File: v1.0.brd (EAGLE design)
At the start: 160 x 100 mm, 53 parts, among them J1 DC-044-A, Q3 6pF@32.7680kHz, U1 MCP23017-E/SO, U10 74HC139N, U2 MCP79412-I/SN, U3 LOPY, U4 GROVE_DC&DC, U5 LM1085IT-5.0, X1 JST-XH-05-PIN-ROUND-PAD, X2 JST-XH-05-PIN-ROUND-PAD, X3 JST-XH-05-PIN-ROUND-PAD, X5 JST-XH-05-PIN-ROUND-PAD

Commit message: very minor tweaks
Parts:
- removed R1: 3K, Seeed-Resistor:R0603
- removed R3: 1K, Seeed-Resistor:R0603
- added TP1: TPB2,54, testpad:B2,54
- moved C10 27.1 mm to (-215.9, -312.4), turned to 180 degrees
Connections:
- removed net N$5: R1.2, R3.1, U5.1
- net +5V: now also C10.+, TP1.TP; no longer C10.-, R3.2
- net GND: now also C10.-, U5.1; no longer C10.+, R1.1
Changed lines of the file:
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@@
 <attribute name="MPN" value="CC0603KRX5R6BB106" x="-229.87" y="-309.88" size="1.778" layer="27" display="off"/>
 </element>
-<element name="R1" library="Seeed-Resistor" library_urn="urn:adsk.eagle:library:474" package="R0603" value="3K" x="-234.95" y="-311.15">
-<attribute name="MPN" value="RC0603FR-073KL" x="-234.95" y="-311.15" size="1.778" layer="27" display="off"/>
+<element name="C10" library="Seeed-Capacitor" library_urn="urn:adsk.eagle:library:464" package="AVX-A" value="10uf" x="-215.9" y="-312.42" rot="R180">
+<attribute name="MPN" value="TAJA106K010RNJ" x="-215.9" y="-312.42" size="1.778" layer="27" rot="R180" display="off"/>
 </element>
-<element name="R3" library="Seeed-Resistor" library_urn="urn:adsk.eagle:library:474" package="R0603" value="1K" x="-240.03" y="-311.15">
-<attribute name="MPN" value="RC0603FR-071KL" x="-240.03" y="-311.15" size="1.778" layer="27" display="off"/>
-</element>
-<element name="C10" library="Seeed-Capacitor" library_urn="urn:adsk.eagle:library:464" package="AVX-A" value="10uf" x="-242.57" y="-317.5">
-<attribute name="MPN" value="TAJA106K010RNJ" x="-242.57" y="-317.5" size="1.778" layer="27" display="off"/>
+<element name="TP1" library="testpad" library_urn="urn:adsk.eagle:library:385" package="B2,54" value="TPB2,54" x="-227.33" y="-318.77">
+<attribute name="TP_SIGNAL_NAME" value="" x="-227.33" y="-318.77" size="1.778" layer="27" display="off"/>
 </element>
 </elements>
@@
 <contactref element="X2" pad="3"/>
 <contactref element="X3" pad="3"/>
-<contactref element="R1" pad="1"/>
 <contactref element="C4" pad="1"/>
-<contactref element="C10" pad="+"/>
+<contactref element="U5" pad="1"/>
+<contactref element="C10" pad="-"/>
 <wire x1="-164.719" y1="-102.87" x2="-160.02" y2="-90.678" width="0" layer="19" extent="1-1"/>
 <wire x1="-148.59" y1="-68.58" x2="-160.02" y2="-90.678" width="0" layer="19" extent="1-1"/>
@@
 <wire x1="-213.36" y1="-241.3" x2="-213.36" y2="-226.06" width="0" layer="19" extent="1-1"/>
 <wire x1="-213.36" y1="-256.54" x2="-213.36" y2="-241.3" width="0" layer="19" extent="1-1"/>
+<wire x1="-217.17" y1="-304.546" x2="-213.36" y2="-256.54" width="0" layer="19" extent="1-1"/>
+<wire x1="-217.17" y1="-312.42" x2="-217.17" y2="-304.546" width="0" layer="19" extent="1-1"/>
+<wire x1="-229.87" y1="-309.118" x2="-217.17" y2="-304.546" width="0" layer="19" extent="1-1"/>
 <wire x1="-114.3" y1="4.572" x2="-129.54" y2="-43.688" width="0" layer="19" extent="1-1"/>
-<wire x1="-229.87" y1="-309.118" x2="-213.36" y2="-256.54" width="0" layer="19" extent="1-1"/>
-<wire x1="-234.95" y1="-310.388" x2="-229.87" y2="-309.118" width="0" layer="19" extent="1-1"/>
-<wire x1="-243.84" y1="-317.5" x2="-234.95" y2="-310.388" width="0" layer="19" extent="1-1"/>
 <wire x1="-86.8934" y1="57.5818" x2="-114.3" y2="4.572" width="0" layer="19" extent="1-1"/>
 <wire x1="-81.8134" y1="55.0418" x2="-86.8934" y2="57.5818" width="0" layer="19" extent="1-1"/>
@@
 <contactref element="X5" pad="1"/>
 <contactref element="U5" pad="2"/>
-<contactref element="R3" pad="2"/>
-<contactref element="C10" pad="-"/>
+<contactref element="C10" pad="+"/>
+<contactref element="TP1" pad="TP"/>
 <wire x1="-214.63" y1="-304.546" x2="-218.44" y2="-287.02" width="0" layer="19" extent="1-1"/>
-<wire x1="-240.03" y1="-311.912" x2="-214.63" y2="-304.546" width="0" layer="19" extent="1-1"/>
-<wire x1="-241.3" y1="-317.5" x2="-240.03" y2="-311.912" width="0" layer="19" extent="1-1"/>
+<wire x1="-214.63" y1="-312.42" x2="-214.63" y2="-304.546" width="0" layer="19" extent="1-1"/>
+<wire x1="-227.33" y1="-318.77" x2="-214.63" y2="-312.42" width="0" layer="19" extent="1-1"/>
 <wire x1="-218.44" y1="-256.54" x2="-218.44" y2="-287.02" width="0" layer="19" extent="1-1"/>
 <wire x1="-218.44" y1="-241.3" x2="-218.44" y2="-256.54" width="0" layer="19" extent="1-1"/>
@@
 <wire x1="-229.87" y1="-310.642" x2="-212.09" y2="-304.546" width="0" layer="19" extent="1-1"/>
 </signal>
-<signal name="N$5">
-<contactref element="U5" pad="1"/>
-<contactref element="R3" pad="1"/>
-<contactref element="R1" pad="2"/>
-<wire x1="-234.95" y1="-311.912" x2="-240.03" y2="-310.388" width="0" layer="19" extent="1-1"/>
-<wire x1="-217.17" y1="-304.546" x2="-234.95" y2="-311.912" width="0" layer="19" extent="1-1"/>
-</signal>
 </signals>

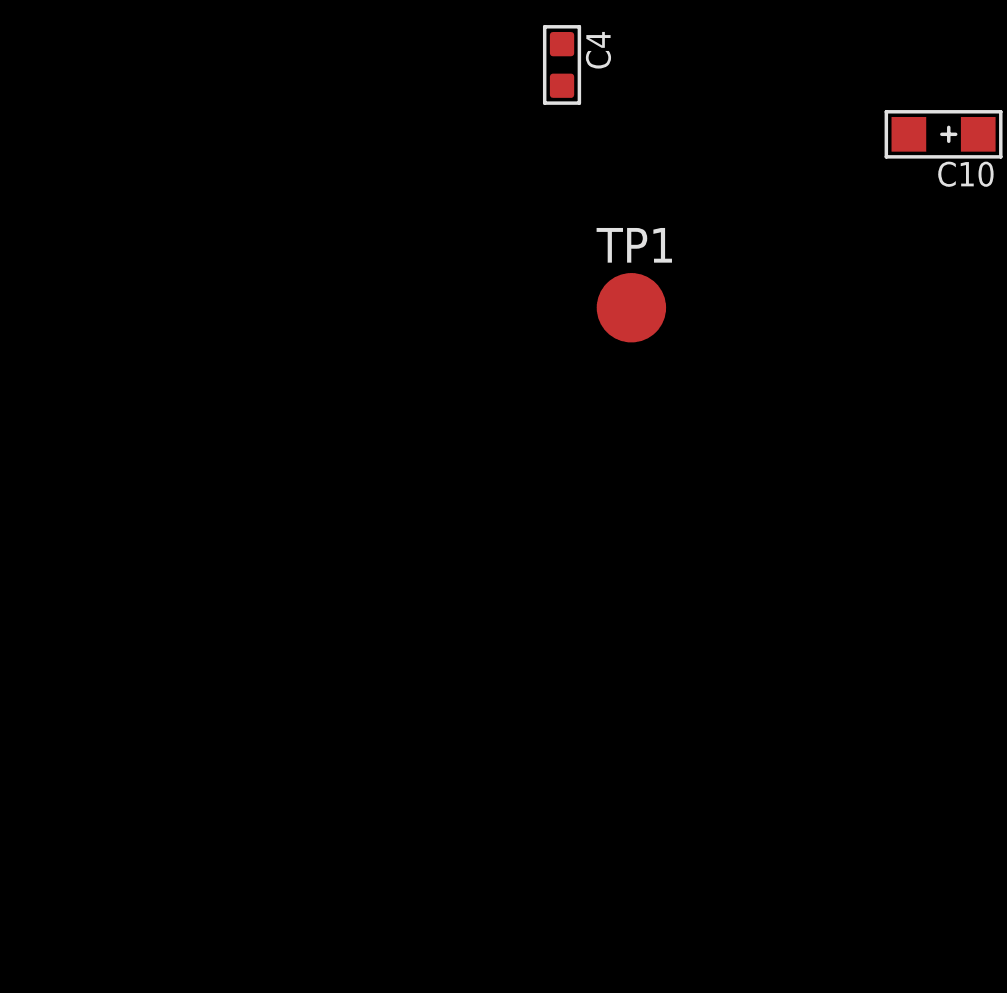
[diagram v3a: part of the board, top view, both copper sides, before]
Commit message: added pycom accessories
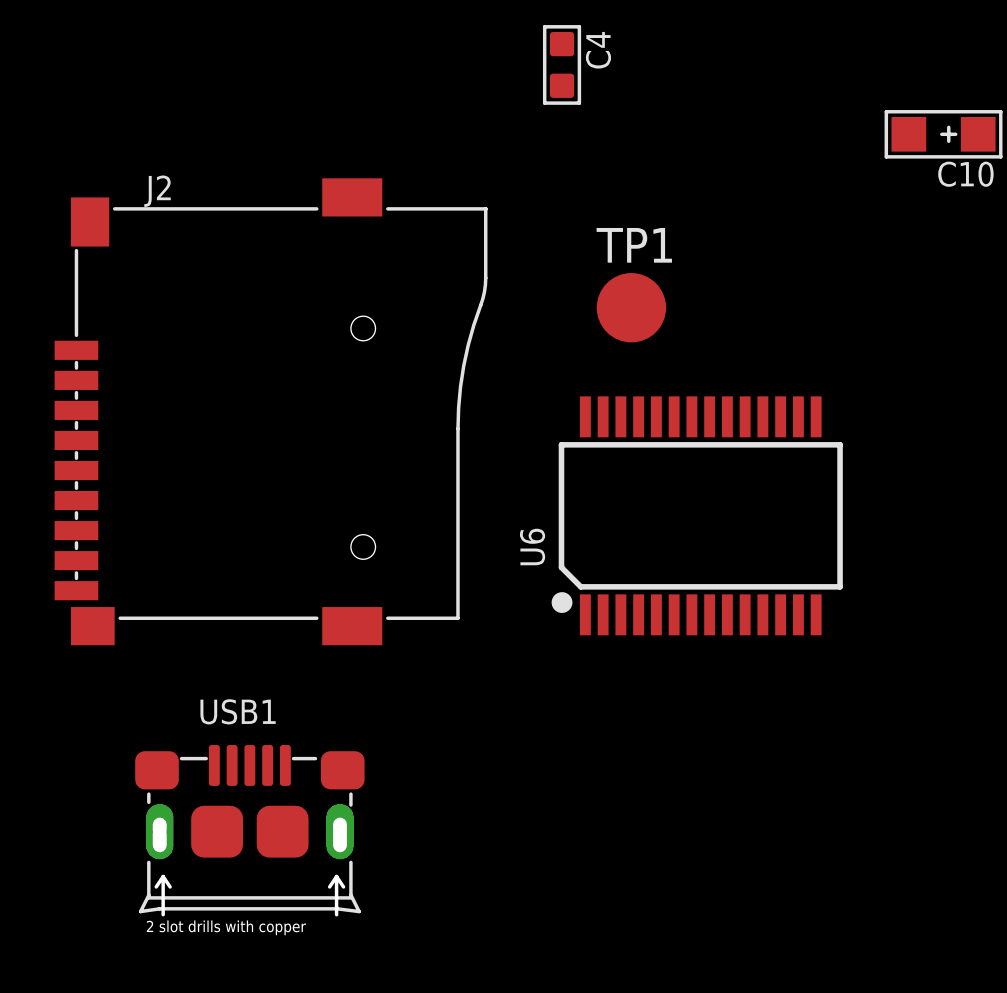
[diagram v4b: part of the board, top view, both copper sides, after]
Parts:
- added J2: MICROSD-9P, Seeed-Connector:MICRO-SD9+4P-SMD-16.1X14.5X1.85MM
- added U6: FT232RL-SSOP28, Seeed-IC:SSOP28-0.65-10.2X5.2MM
- added USB1: 10118193-0001LF, Seeed-Connector:MICRO-USB5+6P-SMD-0.65-B
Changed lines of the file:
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@@
 <attribute name="TP_SIGNAL_NAME" value="" x="-227.33" y="-318.77" size="1.778" layer="27" display="off"/>
+</element>
+<element name="U6" library="Seeed-IC" library_urn="urn:adsk.eagle:library:470" package="SSOP28-0.65-10.2X5.2MM" value="FT232RL-SSOP28" x="-224.79" y="-326.39">
+<attribute name="MPN" value="FT232RL" x="-224.79" y="-326.39" size="1.778" layer="27" display="off"/>
+</element>
+<element name="J2" library="Seeed-Connector" library_urn="urn:adsk.eagle:library:465" package="MICRO-SD9+4P-SMD-16.1X14.5X1.85MM" value="MICROSD-9P" x="-247.65" y="-322.58"/>
+<element name="USB1" library="Seeed-Connector" library_urn="urn:adsk.eagle:library:465" package="MICRO-USB5+6P-SMD-0.65-B" value="10118193-0001LF" x="-241.3" y="-335.28">
+<attribute name="MPN" value="10118193-0001LF" x="-241.3" y="-335.28" size="1.778" layer="27" display="off"/>
 </element>
 </elements>

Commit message: pycom USB
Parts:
- removed X5: JST-XH-05-PIN-ROUND-PAD, Rembrandt Electronics - JST XH Connectors v1-0 2:JST-XH-05-PACKAGE-ROUND-PAD
- added R1: 100K, Seeed-Resistor:R0603
- added X4: JST-XH-07-PIN-ROUND-PAD, Rembrandt Electronics - JST XH Connectors v1-0 2:JST-XH-07-PACKAGE-ROUND-PAD
- moved C4 490.3 mm to (-20.3, 133.3)
- moved C10 481.3 mm to (-25.4, 129.5), turned to 0 degrees
- moved TP1 462.3 mm to (-80.0, 119.4)
- moved USB1 460.9 mm to (-80.0, 96.5)
- moved U5 446.4 mm to (-48.3, 111.8)
- moved U6 440.3 mm to (-94.0, 94.0)
- moved J2 429.1 mm to (-71.1, 68.6)
- moved X3 407.3 mm to (-59.7, 120.7)
- moved C3 405.1 mm to (-15.2, 133.3)
- moved X2 401.0 mm to (-40.6, 120.7)
- moved X1 396.2 mm to (-21.6, 120.7)
- moved C1 357.2 mm to (-115.6, 128.3)
- moved Q3 346.2 mm to (-81.3, 109.2)
- moved C2 328.7 mm to (-120.7, 128.3)
- moved U2 327.1 mm to (-30.5, 110.5)
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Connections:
- removed net +5V/1: USB2.1
- new net LOPY_CS: X4.7
- new net N$5: R1.1, USB1.4
- net +5V: now also USB1.1, USB2.1, X4.1; no longer X5.1
- net GND: now also R1.2, R2.2, USB1.5, USB1.S1, USB1.S2, USB1.S3, USB1.S4, USB1.S5, USB1.S6, USB2.5, USB2.S1, USB2.S2, USB2.S3, USB2.S4, USB2.S5, USB2.S6, X4.3
- net GNDA: no longer R2.2, USB2.5, USB2.S1, USB2.S2, USB2.S3, USB2.S4, USB2.S5, USB2.S6
- net LOPY_3V3: now also X4.2; no longer X5.2
- net LOPY_MISO: now also X4.5; no longer X5.3
- net LOPY_MOSI: now also X4.4; no longer X5.4
- net LOPY_SCL/CLK: now also X4.6; no longer X5.5

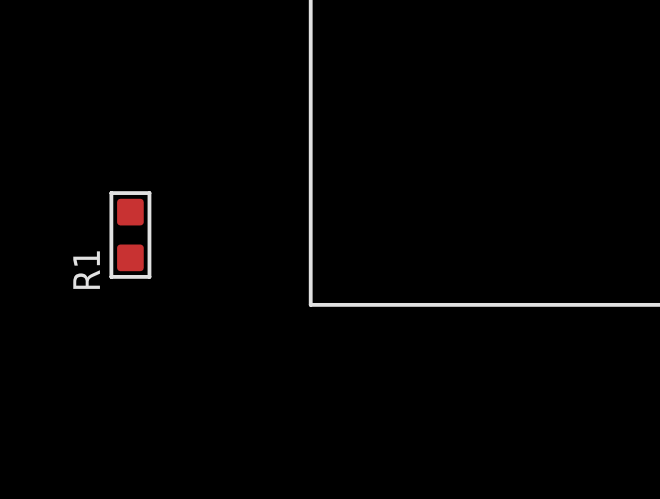
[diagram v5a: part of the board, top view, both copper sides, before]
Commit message: USB to FT23
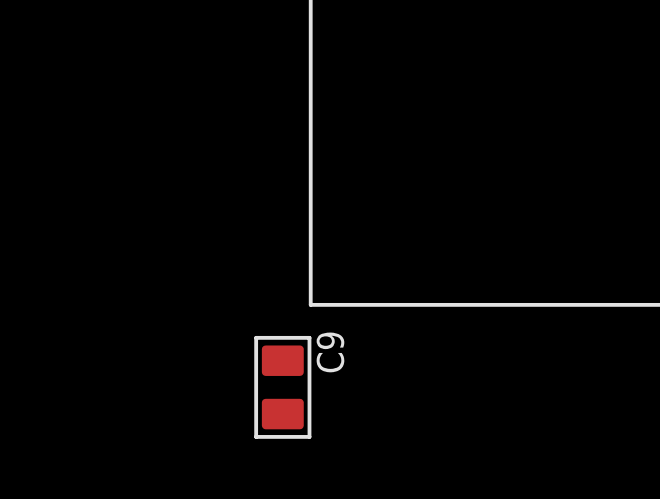
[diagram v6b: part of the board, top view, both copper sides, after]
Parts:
- removed R1: 100K, Seeed-Resistor:R0603
- added C9: 10nf, Seeed-Capacitor:C0805
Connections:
- removed net N$5: R1.1, USB1.4
- new net N$4: USB1.4
- new net N$7: U6.25
- new net USB_DM: U6.16, USB1.2
- new net USB_DP: U6.15, USB1.3
- net +5V: now also C9.1
- net GND: no longer R1.2

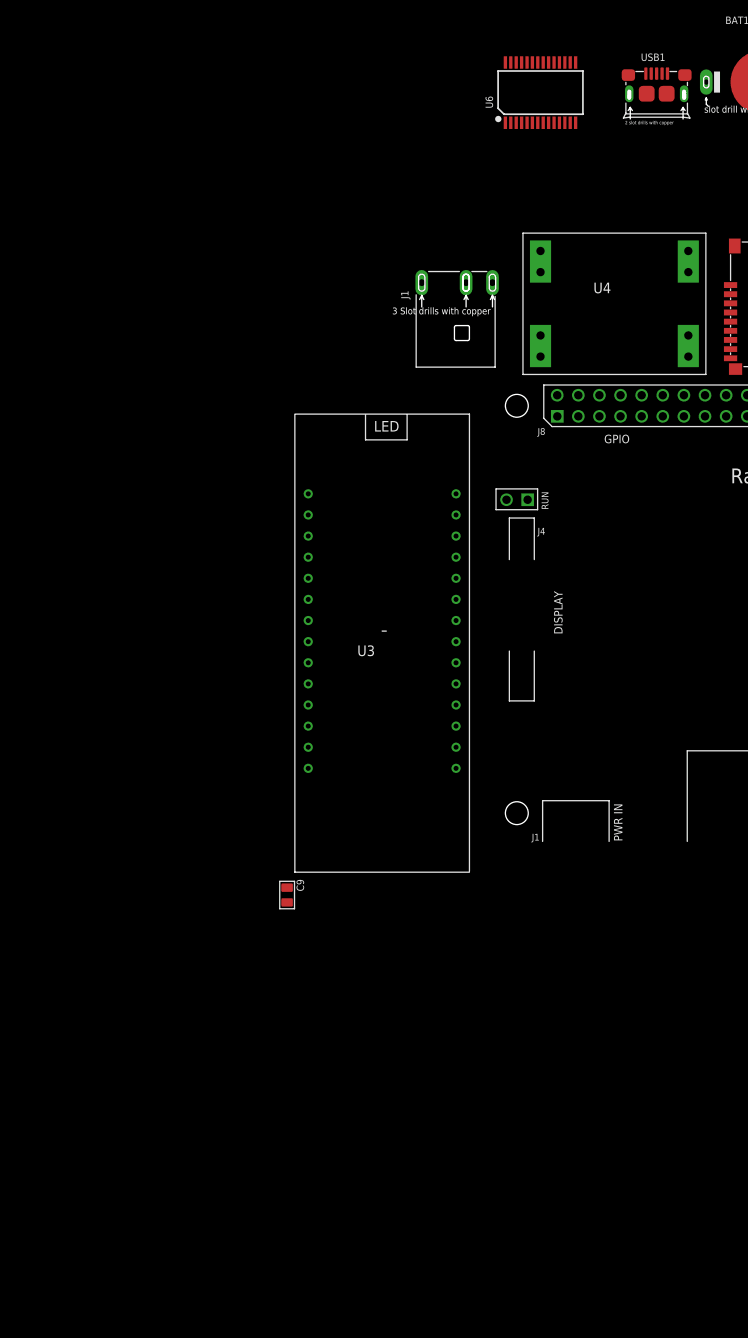
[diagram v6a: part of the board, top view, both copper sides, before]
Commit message: lopy FTDI and SD card socket
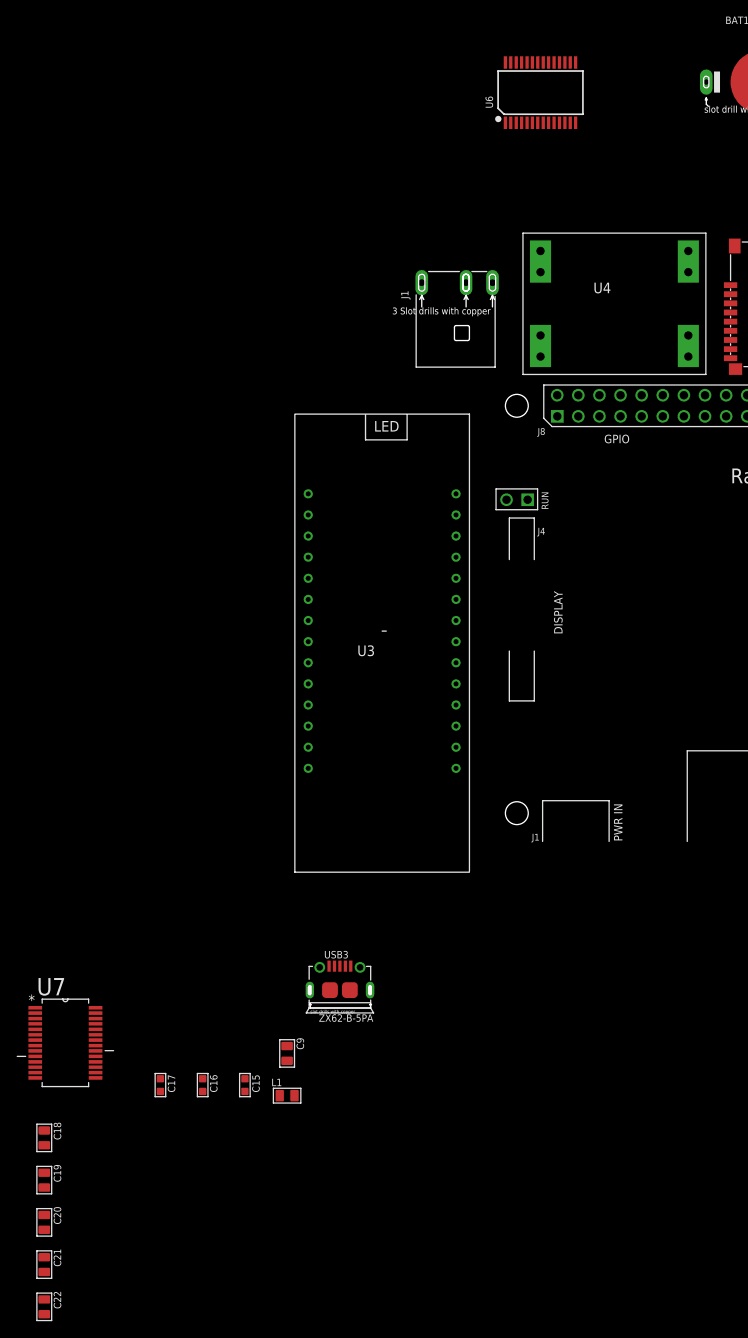
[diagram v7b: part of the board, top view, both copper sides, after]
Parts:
- removed USB1: 10118193-0001LF, Seeed-Connector:MICRO-USB5+6P-SMD-0.65-B
- added C15, C16: 100nf, Seeed-Capacitor-2016:C0603
- added C17: 4.7uf, Seeed-Capacitor-2016:C0603
- added C18, C19, C20, C21, C22: 100nf, Seeed-Capacitor-2016:C0805
- added L1: 330R-1500MA, Seeed-Inductor-2016:L0805
- added U7: MAX213IDBR, ti-max213:SOP65P780X200-28N
- added USB3: ZX62-B-5PA, Seeed-Connector -2016:MICRO-USB5+6P-SMD-0.65-AB
- C9: device Seeed-Capacitor:C0805 -> Seeed-Capacitor-2016:C0805
- moved C9 19.1 mm to (-124.5, -21.6)
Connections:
- new net 3V3_FTDI_OUT: C16.2, U6.17
- new net C1+: C20.2, U7.12
- new net C1-: C20.1, U7.14
- new net C2+: C21.2, U7.15
- new net C2-: C21.1, U7.16
- new net N$18: J2.1
- new net N$20: J2.8
- new net N$21: J2.9
- new net N$24: J2.G1
- new net N$25: J2.G2
- new net N$26: J2.G3
- new net N$27: J2.G4
- new net N$8: USB3.4
- new net SHIELD: USB3.P1, USB3.P2, USB3.P3, USB3.P4, USB3.P5, USB3.P6
- new net SLEEP: U6.12, U7.25
- new net V-: C22.2, U7.17
- new net VBUS: C9.2, L1.1, USB3.1
- net +5V: now also C15.2, C17.2, C18.1, C19.2, L1.2, U6.20, U6.4, U7.11; no longer C9.1, USB1.1
- net GND: now also C15.1, C16.1, C17.1, C18.2, C22.1, C9.1, J2.6, U6.18, U6.21, U6.26, U6.7, U7.10, USB3.5; no longer USB1.5, USB1.S1, USB1.S2, USB1.S3, USB1.S4, USB1.S5, USB1.S6
- net LOPY_3V3: now also J2.4
- net LOPY_CS: now also J2.2
- net LOPY_MISO: now also J2.7
- net LOPY_MOSI: now also J2.3
- net LOPY_SCL/CLK: now also J2.5
- net N$4: now also C19.1, U7.13; no longer USB1.4
- net USB_DM: now also USB3.2; no longer USB1.2
- net USB_DP: now also USB3.3; no longer USB1.3

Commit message: RPI SPI, I2C and UART sockets
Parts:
- added X10, X11, X12, X5, X6, X7, X8, X9: JST-XH-07-PIN-ROUND-PAD, Rembrandt Electronics - JST XH Connectors v1-0 2:JST-XH-07-PACKAGE-ROUND-PAD
- added X13, X14, X15, X16, X17, X18, X19, X20, X21, X22, X23: JST-XH-05-PIN-ROUND-PAD, Rembrandt Electronics - JST XH Connectors v1-0 2:JST-XH-05-PACKAGE-ROUND-PAD
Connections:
- new net RPI_CS1: U10.4, X5.7
- new net RPI_CS2: U10.5, X6.7
- new net RPI_CS3: U10.6, X7.7
- new net RPI_CS4: U10.7, X8.7
- new net RPI_CS5: U10.12, X9.7
- new net RPI_CS6: U10.11, X10.7
- new net RPI_CS7: U10.10, X11.7
- new net RPI_CS8: U10.9, X12.7
- new net SPI_GPIO1: PCB1.P$11, U10.2
- new net SPI_GPIO2: PCB1.P$13, U10.14
- new net SPI_GPIO3: PCB1.P$15, U10.3
- new net SPI_GPIO4: PCB1.P$16, U10.13
- net +3V3: now also X10.2, X11.2, X12.2, X13.2, X14.2, X15.2, X16.2, X17.2, X18.2, X19.2, X20.2, X21.2, X22.2, X23.2, X5.2, X6.2, X7.2, X8.2, X9.2
- net +5V: now also X10.1, X11.1, X12.1, X13.1, X14.1, X15.1, X16.1, X17.1, X18.1, X19.1, X20.1, X21.1, X22.1, X23.1, X5.1, X6.1, X7.1, X8.1, X9.1
- net GND: now also X10.3, X11.3, X12.3, X13.3, X14.3, X15.3, X16.3, X17.3, X18.3, X19.3, X20.3, X21.3, X22.3, X23.3, X5.3, X6.3, X7.3, X8.3, X9.3
- net SCL_3V3: now also X13.5, X14.5, X15.5, X16.5, X17.5, X18.5, X19.5, X20.5, X21.5, X22.5
- net SDA_3V3: now also X13.4, X14.4, X15.4, X16.4, X17.4, X18.4, X19.4, X20.4, X21.4, X22.4
- net SPI_MISO: now also X10.4, X11.5, X12.4, X5.4, X6.4, X7.4, X8.5, X9.4
- net SPI_MOSI: now also X10.5, X11.4, X12.5, X5.5, X6.5, X7.5, X8.4, X9.5
- net SPI_SCLK: now also X10.6, X11.6, X12.6, X5.6, X6.6, X7.6, X8.6, X9.6
- net UART_RX: now also X23.5
- net UART_TDX: now also X23.4
